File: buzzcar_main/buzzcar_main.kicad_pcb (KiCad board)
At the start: 2 copper layers, 154.9 x 76.2 mm, 35 parts, among them J1 9V Battery Cap, J10 Sensor_B, J11 Sensor_A, J2 5V Buck, J3 3.3V Buck, J4 Motor_A, J5 Motor_B, J6 Video GME12864, J7 Audio Amp PAM8904, J8 8Ω Speaker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

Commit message: PCB Layout v0.2 done - silkscreen errors left
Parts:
- added J12: Safety, Connector_PinHeader_2.54mm:PinHeader_1x05_P2.54mm_Vertical, F.Cu at (120.1, 85.6)
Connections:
- U1 pad 3: unconnected-(U1-GPIO4/MTMS-Pad3) -> Net-(J12-Pin_5)
- U1 pad 4: unconnected-(U1-GPIO5/MTDI-Pad4) -> Net-(J12-Pin_4)
- U1 pad 5: unconnected-(U1-GPIO6-Pad5) -> Net-(J12-Pin_3)
- U1 pad 6: unconnected-(U1-GPIO7-Pad6) -> Net-(J12-Pin_2)
- U1 pad 7: unconnected-(U1-GPIO0-Pad7) -> Net-(J12-Pin_1)
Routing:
- net Net-(J12-Pin_5): track 0.00 -> 59.8 mm
- net GND: track 493.1 -> 549.9 mm, vias 0 -> 2
- net Net-(J12-Pin_4): track 0.00 -> 56.2 mm
- net Net-(J12-Pin_3): track 0.00 -> 52.6 mm
- net Net-(J12-Pin_2): track 0.00 -> 49.0 mm
- net Net-(J12-Pin_1): track 0.00 -> 45.4 mm
- net /spk_sig: track 80.1 -> 83.8 mm
- net /sig_c: track 93.0 -> 91.5 mm
- net /i2c_scn_scl: track 67.5 -> 68.4 mm

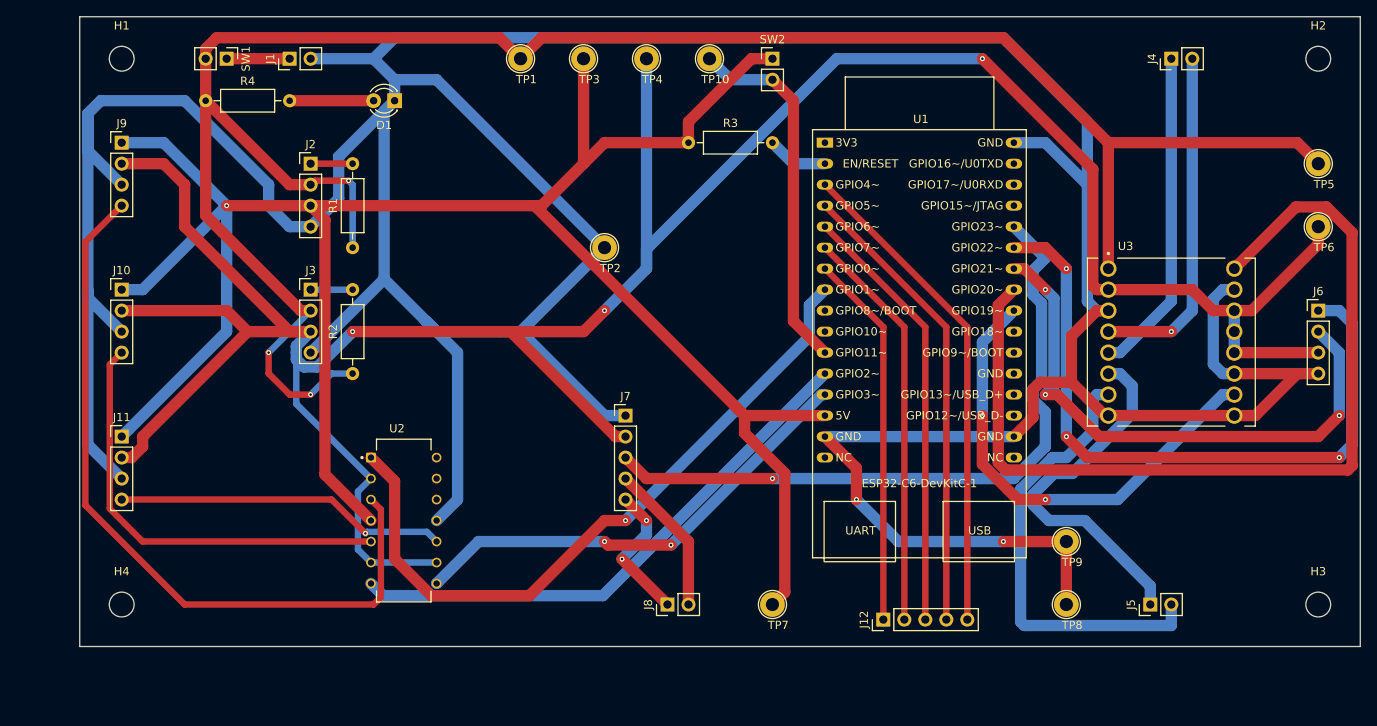
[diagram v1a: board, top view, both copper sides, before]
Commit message: PCB v0.3 ready - fixed PCB traces, fixed crossing over into margins of drill holes
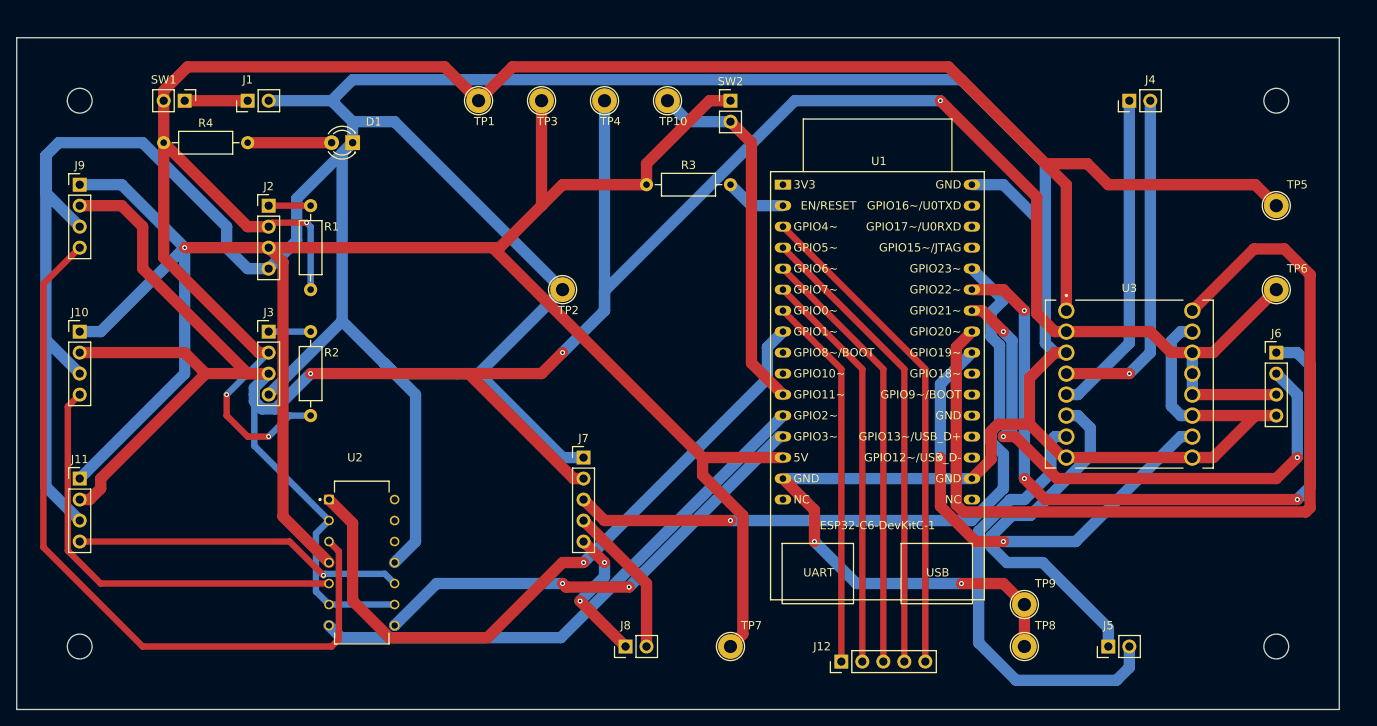
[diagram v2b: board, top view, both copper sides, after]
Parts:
- moved TP6 9.16 mm to (167.6, 45.7)
- moved TP9 9.16 mm to (137.2, 83.8)
- moved H3 7.18 mm to (167.6, 88.9)
- moved J5 7.18 mm to (147.3, 88.9)
- moved TP7 7.18 mm to (101.6, 88.9)
- moved TP8 7.18 mm to (137.2, 88.9)
- moved J6 7.18 mm to (167.6, 53.3)
- moved J7 7.18 mm to (83.8, 66.0)
- moved H4 7.18 mm to (22.9, 88.9)
- moved TP5 7.18 mm to (167.6, 35.6)
- moved H2 7.18 mm to (167.6, 22.9)
- moved J8 7.18 mm to (88.9, 88.9)
- moved SW2 7.18 mm to (101.6, 22.9)
- moved J9 7.18 mm to (22.9, 33.0)
- moved R1 7.18 mm to (50.8, 45.7)
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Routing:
- net +9V: track 248.5 -> 254.6 mm
- net GND: track 549.9 -> 547.4 mm
- net +3.3V: track 349.9 -> 347.6 mm
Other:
- board size 154.9 x 76.2 mm -> 160 x 81.3 mm

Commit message: Added silkscreen annotations, reduced board size to within 15cm x 15cm
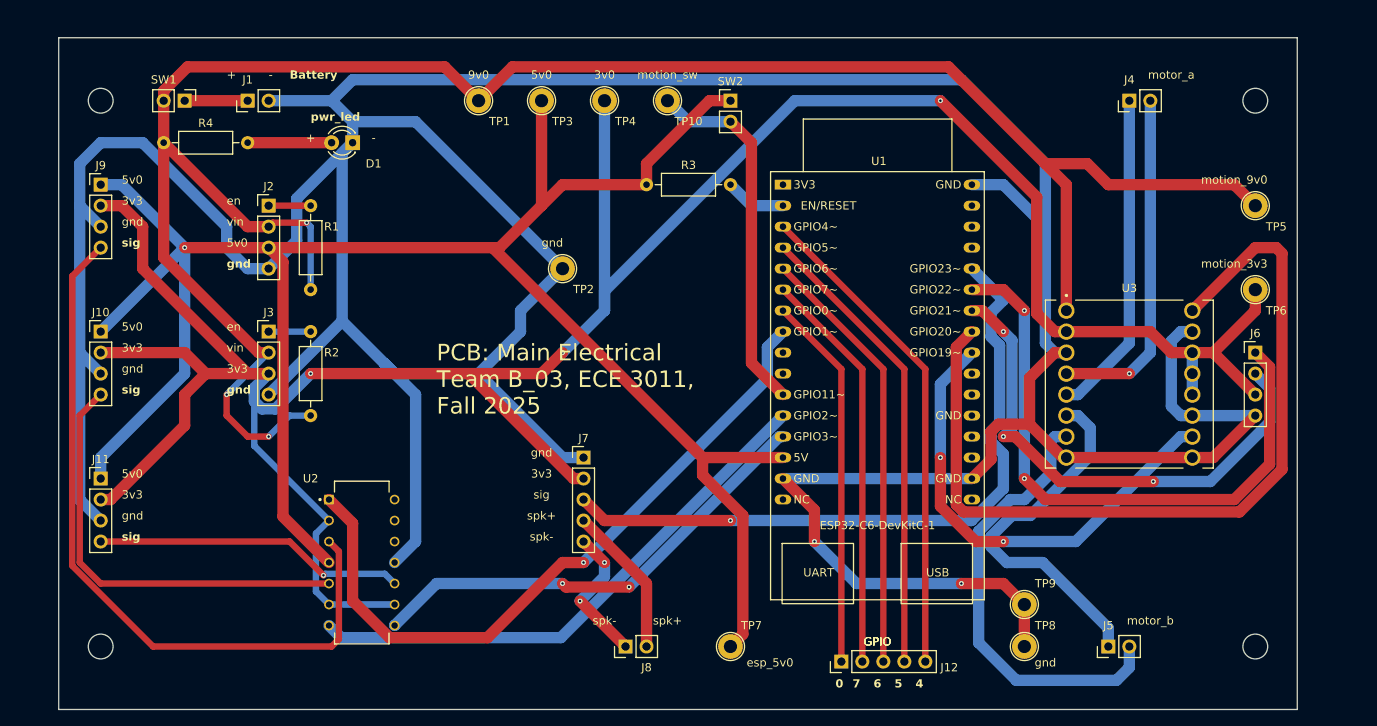
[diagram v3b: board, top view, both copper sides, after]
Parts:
- moved H1 2.54 mm to (25.4, 22.9)
- moved H4 2.54 mm to (25.4, 88.9)
- moved J10 2.54 mm to (25.4, 50.8)
- moved J11 2.54 mm to (25.4, 68.6)
- moved J9 2.54 mm to (25.4, 33.0)
- moved TP2 2.54 mm to (81.3, 43.2)
- moved H2 2.54 mm to (165.1, 22.9)
- moved H3 2.54 mm to (165.1, 88.9)
- moved J6 2.54 mm to (165.1, 53.3)
- moved TP5 2.54 mm to (165.1, 35.6)
- moved TP6 2.54 mm to (165.1, 45.7)
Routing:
- net GND: track 547.4 -> 532.2 mm
- net +3.3V: track 347.6 -> 337.4 mm
- net /i2c_scn_sda: track 83.4 -> 74.4 mm, vias 3 -> 2
- net /motor_a_pwm: track 111.9 -> 104.1 mm
- net +5V: track 265.8 -> 259.7 mm
- net /i2c_scn_scl: track 68.4 -> 62.5 mm
- net /sig_c: track 91.5 -> 88.9 mm
- net +9V: track 254.6 -> 252.1 mm
- net /sig_a: track 40.4 -> 37.8 mm
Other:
- board size 160 x 81.3 mm -> 149.9 x 81.3 mm
- board text added: "+"
- board text added: "-"
- board text added: "0"
- board text added: "3v0"
- board text added: "3v3"
- board text added: "4"
- board text added: "5"
- board text added: "5v0"
- board text added: "6"
- board text added: "7"
- board text added: "9v0"
- board text added: "Battery"
- board text added: "GPIO"
- board text added: "PCB: Main Electrical Team B_03, ECE 3011, Fall 2025"
- board text added: "en"
- board text added: "esp_5v0"
- board text added: "gnd"
- board text added: "motion_3v3"
- board text added: "motion_9v0"
- board text added: "motion_sw"
- board text added: "motor_a"
- board text added: "motor_b"
- board text added: "pwr_led"
- board text added: "sig"
- board text added: "spk+"
- board text added: "spk-"
- board text added: "vin"

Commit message: Buzzcar Control Board v1.0 complete
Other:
- board text added: "Allen"
- board text added: "Buzzcar Control Board v1.0"
- board text added: "ECE3011, Fall 2025"
- board text added: "Justin"
- board text added: "Preston"
- board text added: "Sec B, Team 3"
- board text added: "Ved"
- board text added: "When I was a young boy"
- board text removed: "PCB: Main Electrical Team B_03, ECE 3011, Fall 2025"
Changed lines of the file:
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@@
 		(tags "Through hole pin header THT 1x05 2.54mm single row")
 		(property "Reference" "J12"
-			(at -0.715 11.985 180)
+			(at 1.825 11.985 180)
 			(layer "F.SilkS")
 			(effects
@@
 		(layer "Edge.Cuts")
 	)
-	(gr_text "GPIO"
-		(at 119.38 88.9 0)
-		(layer "F.SilkS")
-		(effects
-			(font
-				(size 1 1)
-				(thickness 0.15)
-			)
-			(justify bottom)
+	(gr_text "When I was a young boy"
+		(at 167.64 17.78 0)
+		(layer "B.SilkS")
+		(effects
+			(font
+				(size 1 1)
+				(thickness 0.15)
+			)
+			(justify left bottom mirror)
+		)
+	)
+	(gr_text "Preston"
+		(at 149.86 33.02 0)
+		(layer "B.SilkS")
+		(effects
+			(font
+				(size 1 1)
+				(thickness 0.15)
+			)
+			(justify left bottom mirror)
+		)
+	)
+	(gr_text "Allen"
+		(at 149.86 27.94 0)
+		(layer "B.SilkS")
+		(effects
+			(font
+				(size 1 1)
+				(thickness 0.15)
+			)
+			(justify left bottom mirror)
+		)
+	)
+	(gr_text "Ved"
+		(at 149.86 35.56 0)
+		(layer "B.SilkS")
+		(effects
+			(font
+				(size 1 1)
+				(thickness 0.15)
+			)
+			(justify left bottom mirror)
+		)
+	)
+	(gr_text "Justin"
+		(at 149.86 30.48 0)
+		(layer "B.SilkS")
+		(effects
+			(font
+				(size 1 1)
+				(thickness 0.15)
+			)
+			(justify left bottom mirror)
 		)
 	)
@@
 		)
 	)
+	(gr_text "Sec B, Team 3"
+		(at 167.64 83.82 90)
+		(layer "F.SilkS")
+		(effects
+			(font
+				(size 1.5 1.5)
+				(thickness 0.3)
+				(bold yes)
+			)
+			(justify left bottom)
+		)
+	)
 	(gr_text "sig"
 		(at 78.74 71.12 0)
@@
 		)
 	)
-	(gr_text "motion_sw"
-		(locked yes)
-		(at 93.98 20.32 0)
-		(layer "F.SilkS")
-		(effects
-			(font
-				(size 1 1)
-				(thickness 0.1)
-			)
-			(justify bottom)
-		)
-	)
 	(gr_text "5v0"
 		(at 78.74 20.32 0)
@@
 		)
 	)
+	(gr_text "motion_sw"
+		(at 91.44 20.32 0)
+		(layer "F.SilkS")
+		(effects
+			(font
+				(size 1 1)
+				(thickness 0.15)
+			)
+			(justify left bottom)
+		)
+	)
 	(gr_text "0"
 		(at 114.3 93.98 0)
@@
 		)
 	)
-	(gr_text "GPIO"
-		(at 119.38 88.9 0)
-		(layer "F.SilkS")
-		(effects
-			(font
-				(size 1 1)
-				(thickness 0.15)
-			)
-			(justify bottom)
-		)
-	)
-	(gr_text "PCB: Main Electrical\nTeam B_03, ECE 3011, \nFall 2025"
-		(at 66.04 60.96 0)
-		(layer "F.SilkS")
-		(effects
-			(font
-				(size 2 2)
-				(thickness 0.3)
+	(gr_text "Buzzcar Control Board v1.0"
+		(at 30.48 93.98 0)
+		(layer "F.SilkS")
+		(effects
+			(font
+				(size 2.5 2.5)
+				(thickness 0.4)
 			)
 			(justify left bottom)
@@
 		)
 	)
-	(gr_text "GPIO"
-		(at 119.38 88.9 0)
-		(layer "F.SilkS")
-		(effects
-			(font
-				(size 1 1)
-				(thickness 0.15)
-			)
-			(justify bottom)
-		)
-	)
 	(gr_text "sig\n"
 		(at 27.94 40.64 0)
@@
 		)
 	)
+	(gr_text "GPIO"
+		(at 127 93.98 0)
+		(layer "F.SilkS")
+		(effects
+			(font
+				(size 1 1)
+				(thickness 0.15)
+			)
+			(justify left bottom)
+		)
+	)
 	(gr_text "9v0"
 		(at 71.12 20.32 0)
@@
 		)
 	)
+	(gr_text "ECE3011, Fall 2025"
+		(at 114.3 20.32 0)
+		(layer "F.SilkS")
+		(effects
+			(font
+				(size 1.5 1.5)
+				(thickness 0.3)
+				(bold yes)
+			)
+			(justify left bottom)
+		)
+	)
